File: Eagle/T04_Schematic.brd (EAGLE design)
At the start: 36.5 x 59.7 mm, 26 parts, among them Y1 16 MHz

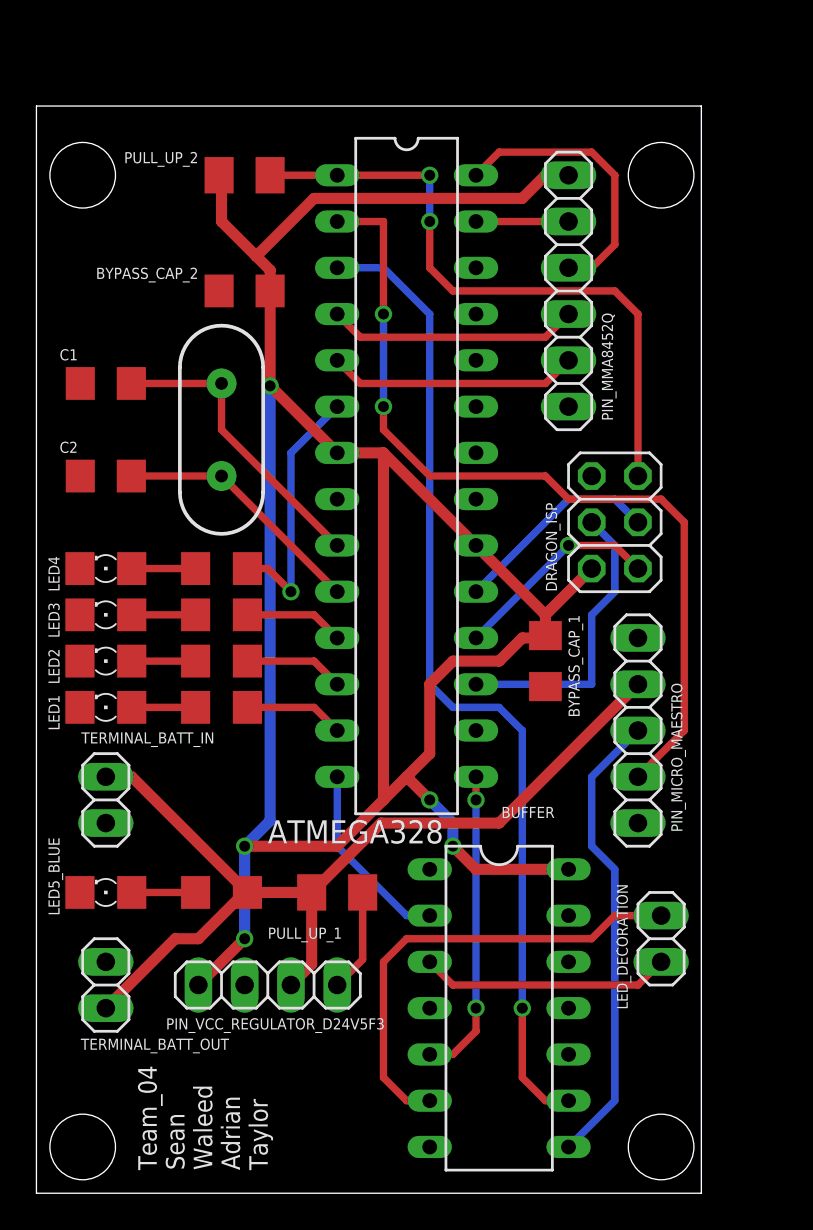
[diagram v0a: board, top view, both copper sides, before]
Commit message: DRC Error Free Layout + Schematic Update
Made changes to layout based on feedback from class.
Added linear regulator to schematic for 5V supply.
Will need group review.
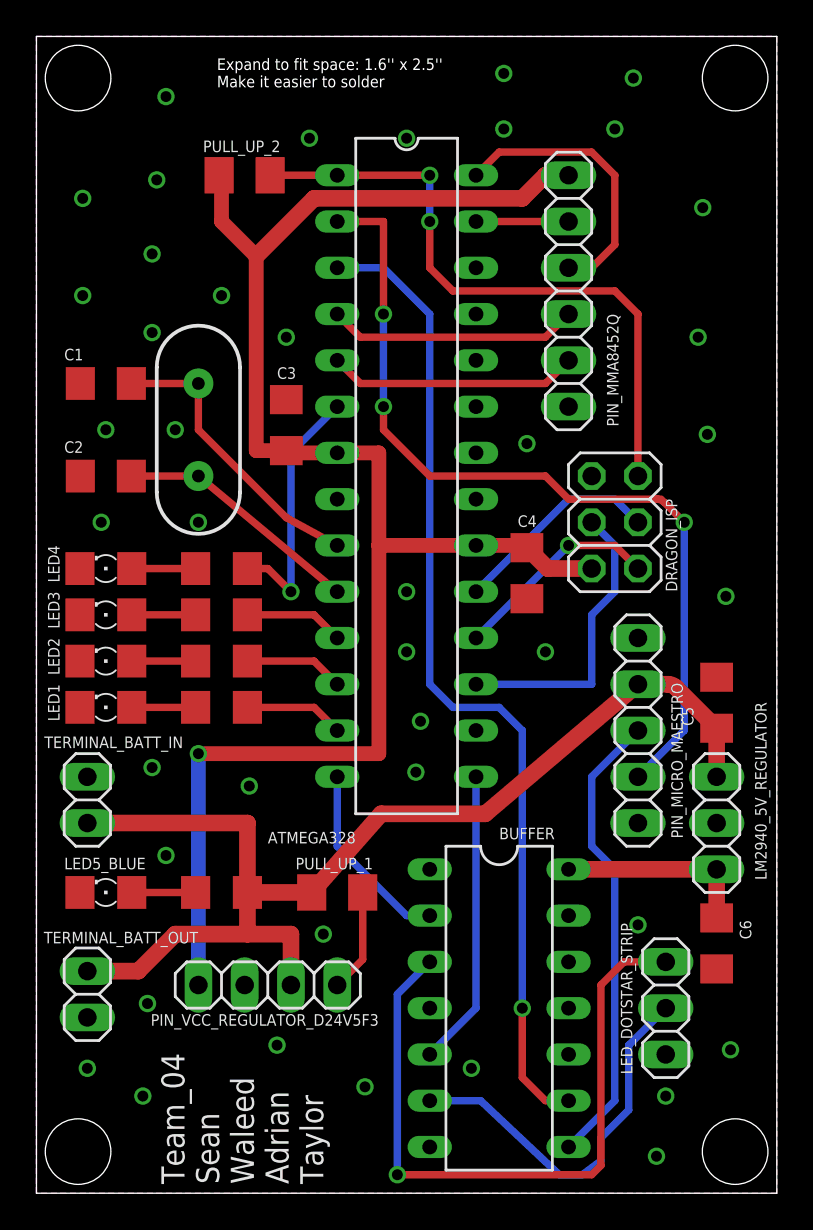
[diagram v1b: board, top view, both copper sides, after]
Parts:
- removed BYPASS_CAP_1, BYPASS_CAP_2: 100 nF, rcl:C1206
- removed LED_DECORATION: 1x2, pinhead:1X02
- added C3, C4: 100 nF, rcl:C1206
- added C5: .47uF, rcl:C1206
- added C6: 22uF, rcl:C1206
- added LED_DOTSTAR_STRIP: 1x3, pinhead:1X03
- added LM2940_5V_REGULATOR: (no value), pinhead:1X03
- moved Y1 1.27 mm to (8.89, 41.9)
- moved TERMINAL_BATT_OUT 1.14 mm to (2.79, 10.9), turned to 270 degrees
- moved TERMINAL_BATT_IN 1.02 mm to (2.79, 21.6), turned to 270 degrees
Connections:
- new net 5V_VCC: BUFFER.14, C6.1, LM2940_5V_REGULATOR.3
- net GND: now also C3.2, C4.2, C5.2, C6.2, LED_DOTSTAR_STRIP.3, LM2940_5V_REGULATOR.2; no longer BYPASS_CAP_1.2, BYPASS_CAP_2.2
- net N$13: now also LED_DOTSTAR_STRIP.2; no longer LED_DECORATION.2
- net N$8: now also LED_DOTSTAR_STRIP.1; no longer LED_DECORATION.1
- net VCC: now also C3.1, C4.1; no longer BUFFER.14, BYPASS_CAP_1.1, BYPASS_CAP_2.1
- net VCC_6V: now also C5.1, LM2940_5V_REGULATOR.1
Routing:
- net VCC: track 145.8 -> 93.1 mm, vias 5 -> 1
- net N$8: track 13.8 -> 37.8 mm, vias 0 -> 1
- net VCC_6V: track 52.5 -> 63.6 mm
- net 5V_VCC: track 0.00 -> 10.8 mm
- net N$13: track 25.7 -> 21.1 mm
- net DATA: track 17.0 -> 16.3 mm, vias 2 -> 0
- net SERVO_TXD: track 47.6 -> 47.8 mm, vias 2 -> 3
- added copper zone on layer 1, net GND
- added copper zone on layer 16, net GND
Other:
- board size 36.5 x 59.7 mm -> 40.6 x 63.5 mm
- board text added: "Expand to fit space: 1.6'' x 2.5'' Make it easier to solder"
